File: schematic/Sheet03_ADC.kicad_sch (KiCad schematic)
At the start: 5 parts

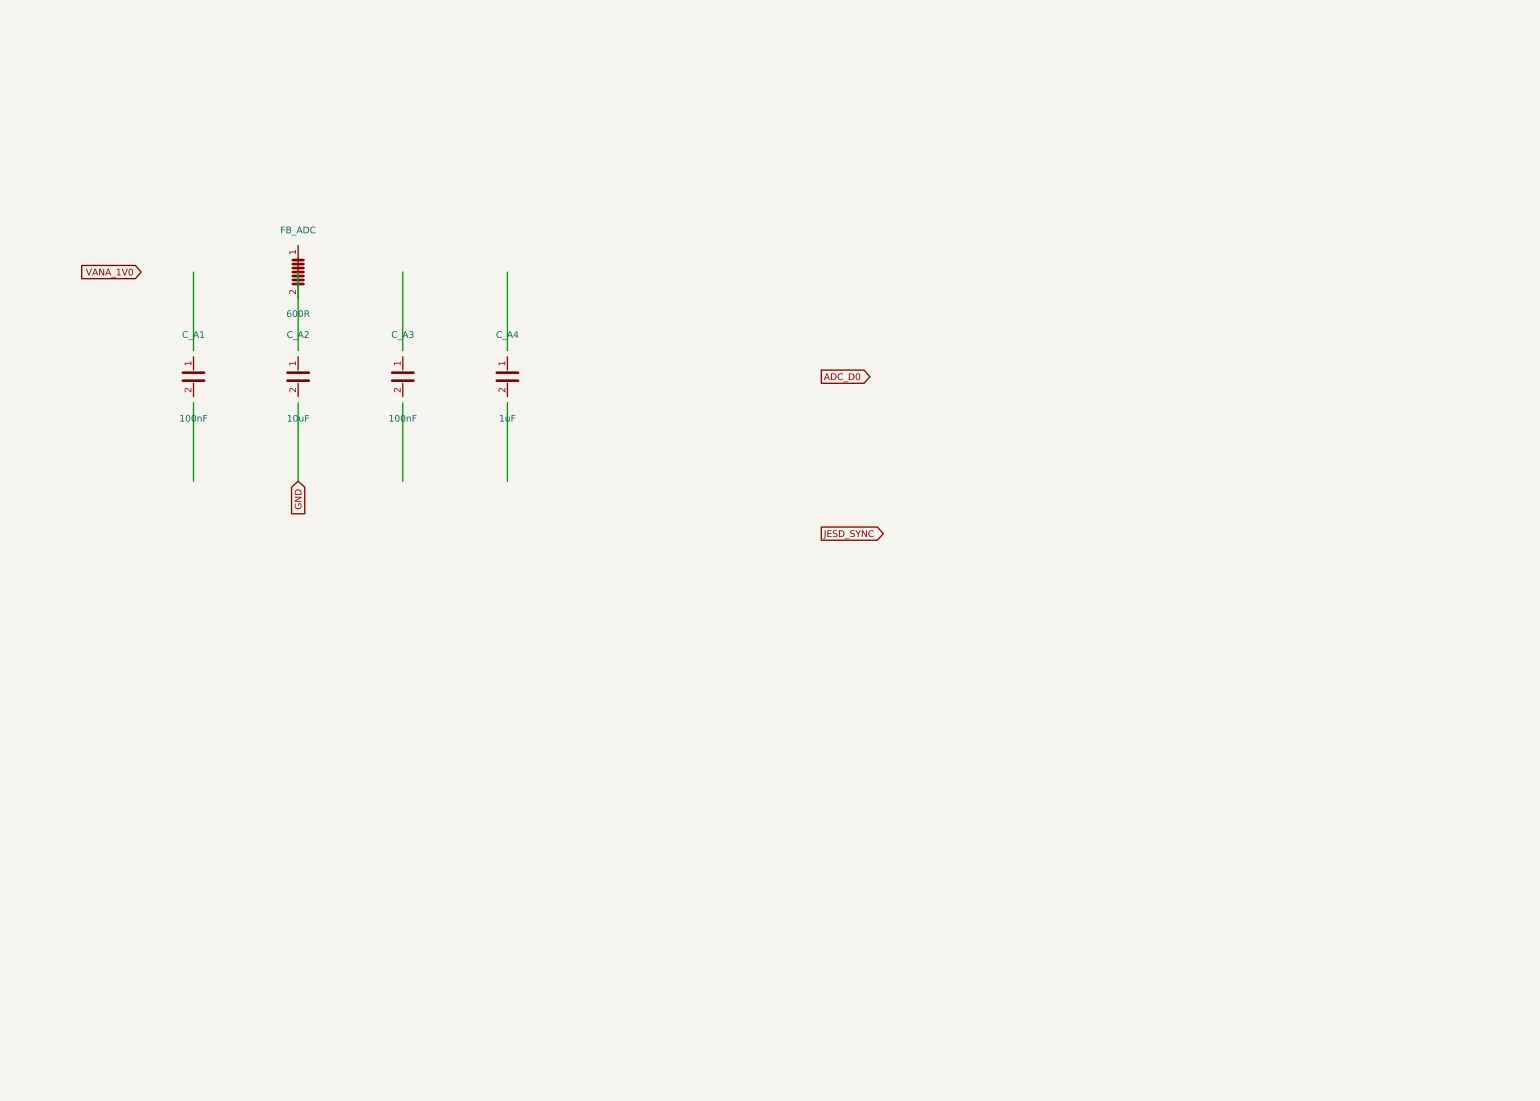
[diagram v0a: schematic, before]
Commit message: feat: real IC schematics with proper pin connections
- ADC12DJ5200-SP: 20 left pins (power, SPI, analog) + 21 right pins (JESD204C)
- XQRVC1902-SP: 19 left pins (power) + 30 right pins (JTAG, SPW, JESD, config)
- TPS7H5002-SP: 9 left + 7 right pins (buck converter 1.0V core)
- ISL70003ASEH: 7 left + 5 right (buck 1.8V/3.3V)
- LMX2615-SP: 8+8 pins (PLL synthesizer)
- LMK04832-SP: 12+12 pins (clock distributor)
- TPS7H1111-SP / TPS7H1121-SP: 3+3 pins (LDOs)
- TPS7H3014-SP: 4+4 pins (sequencer)
- INA214-SP: 3+2 pins (current sense)
- CVHD-950: 3+2 pins (VCXO)

Sheets:
- 02: SMA→50Ω match→anti-alias→ADC analog input
- 03: ADC decoupling, JESD outputs, SPI control
- 04: FPGA 14x decoupling caps, JTAG, SPW, JESD
- 05: Crystek→LMX2615→LMK04832→ADC+FPGA clock tree
- 06-09: Power input, TPS7H5002 buck 1.0V, ISL70003A buck 1.8V/3.3V
- 10-12: LDO 1.0V analog, 1.8V digital, 2.5V clock
- 13: 2x TPS7H3014 power sequencer
- 14: JTAG/SPW/UART connectors
- 15-17: Test points, decoupling, power tree diagram

All 17 sheets export via kicad-cli, merged PDF: 1.1MB
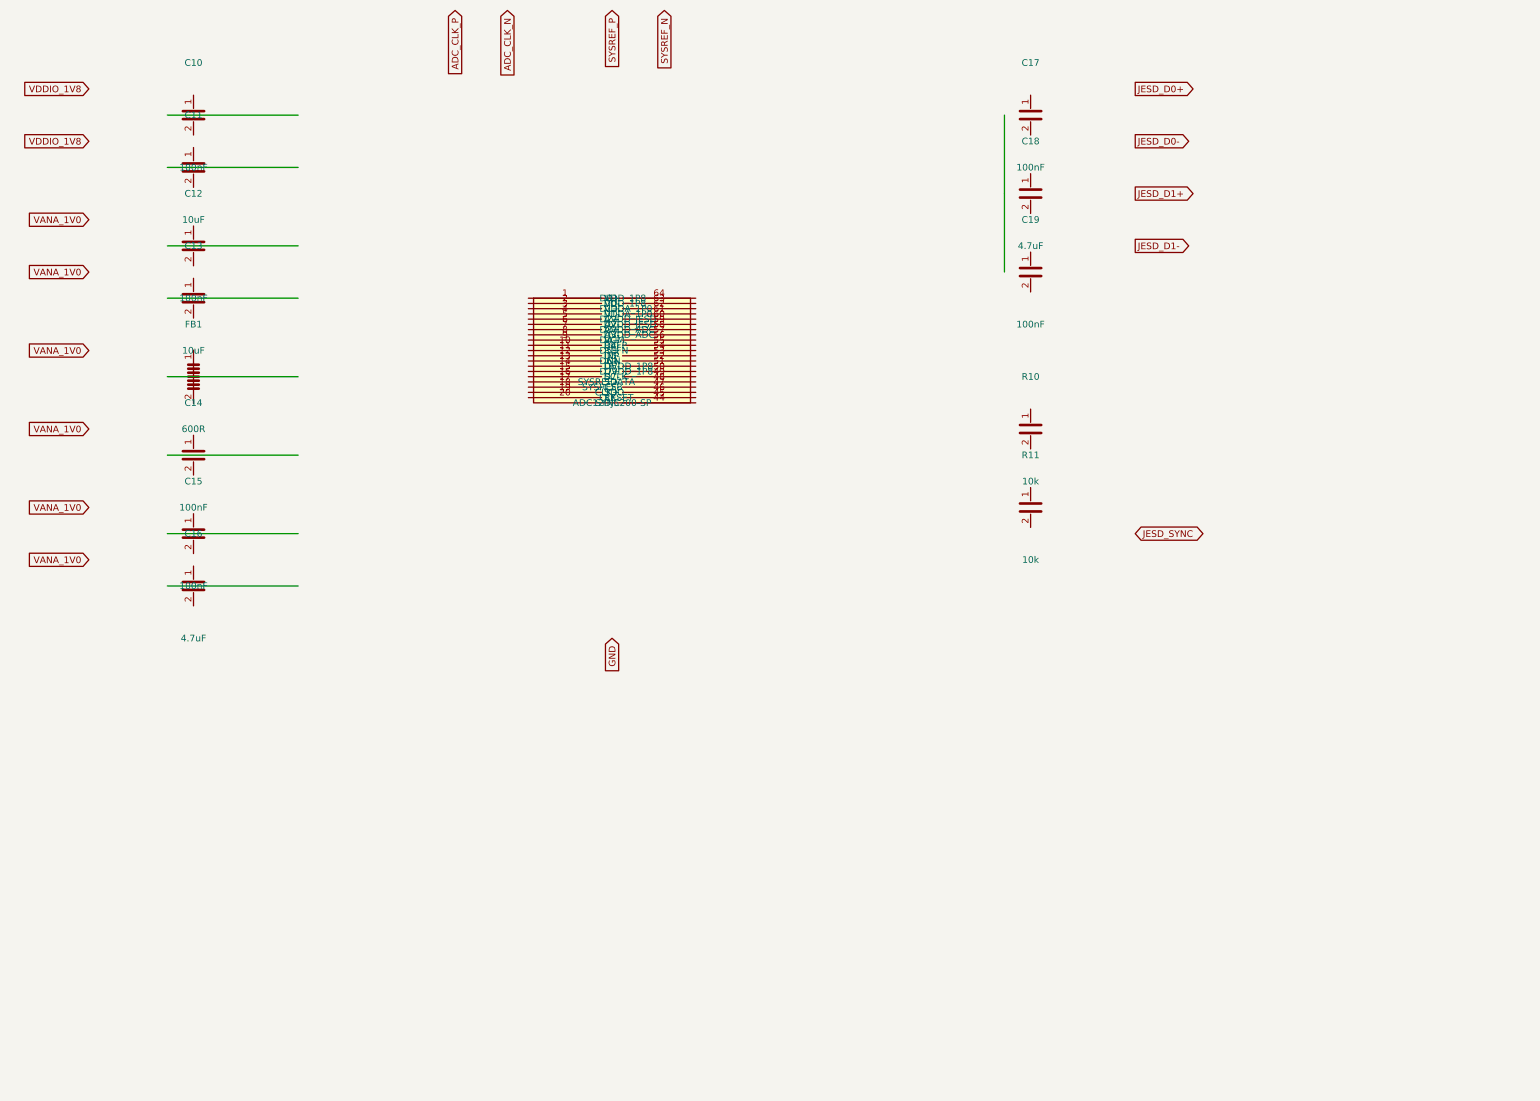
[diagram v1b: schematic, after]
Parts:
- removed C_A1, C_A3: 100nF, Capacitor_SMD:C_0402_1005Metric, symbol Device:C
- removed C_A2: 10uF, Capacitor_SMD:C_0603_1608Metric, symbol Device:C
- removed C_A4: 1uF, Capacitor_SMD:C_0402_1005Metric, symbol Device:C
- removed FB_ADC: 600R, Inductor_SMD:L_0402_1005Metric, symbol Device:FerriteBead
- added C10, C12, C14, C15, C17, C19: 100nF, C_0402, symbol Device:C
- added C11, C13: 10uF, C_0603, symbol Device:C
- added C16, C18: 4.7uF, C_0402, symbol Device:C
- added FB1: 600R, L_0402, symbol Device:FerriteBead
- added R10, R11: 10k, C_0402, symbol Device:C
- added U1: ADC12DJ5200-SP, QFN-64, symbol Custom:ADC12DJ5200-SP
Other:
- title: X-Band Digital Module 20x20cm -> X-Band ADC12DJ5200-SP

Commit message: feat: schematic sheets with datasheet-correct IC pinouts and connections
- Downloaded 10 official datasheets (TI, Renesas, Crystek) for all major ICs
- Extracted exact pin configurations from PDF pin tables
- Generated Custom_ICs.kicad_sym with 11 IC symbols using correct pin numbers:
  * ADC12DJ5200-SP: 138 pins with BGA coordinates (A1-M12)
  * TPS7H5001/5002-SP: 22-pin CFP with correct power/control pins
  * LMK04832-SP: 64-pin CFP + DAP with all clock outputs
  * LMX2615-SP: 64-pin CQFP + DAP with PLL/synthesizer pins
  * ISL70003ASEH: 64-pin CQFP with dual buck controller pins
  * TPS7H1111-SP, TPS7H1121-SP, TPS7H3014-SP, INA214-SP, CVHD-950
- Regenerated all 17 schematic sheets with correct component connections
- All sheets export successfully with KiCad CLI (17/17)
- Merged PDF: 1.3MB, 17 pages
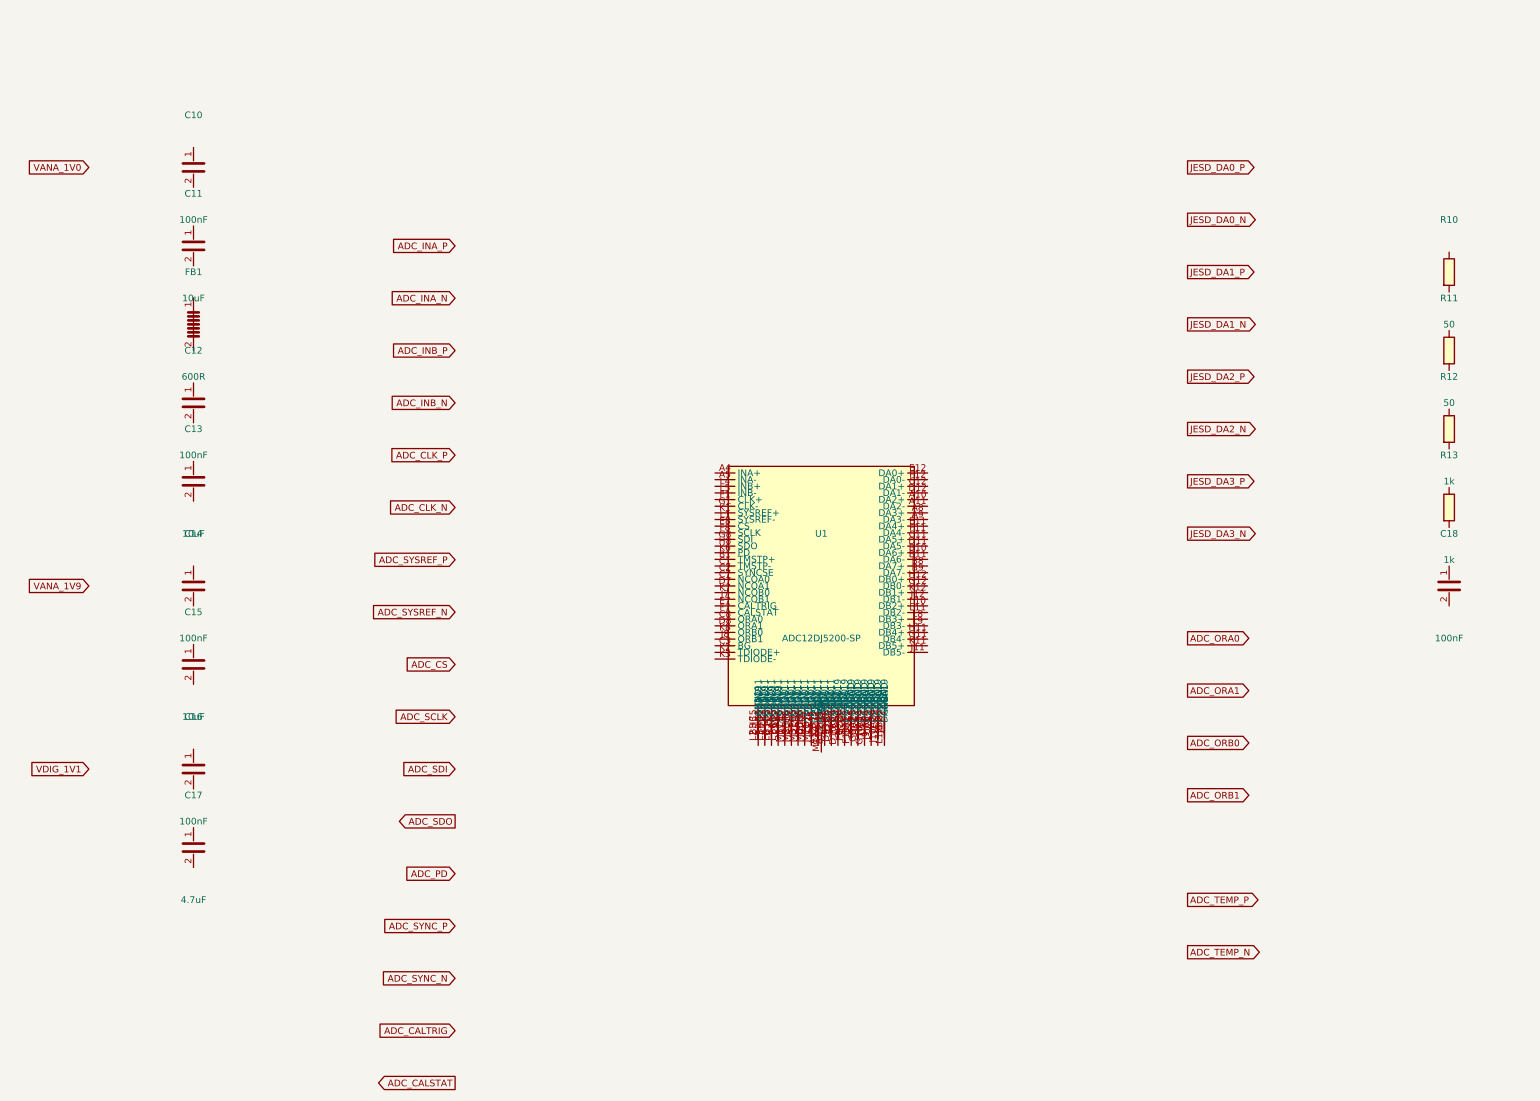
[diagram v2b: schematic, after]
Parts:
- removed C19: 100nF, C_0402, symbol Device:C
- removed R10, R11: 10k, C_0402, symbol Device:C
- added R10, R11: 50, R_0402, symbol Device:R
- added R12, R13: 1k, R_0402, symbol Device:R
- C15: value 100nF -> 10uF; footprint C_0402 -> C_0603
- C16, C18: value 4.7uF -> 100nF
- C17: value 100nF -> 4.7uF
- U1: footprint QFN-64 -> Package_BGA:BGA-144_12x12_8.0x8.0mm_P0.65mm

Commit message: feat: add 745 wire connections linking all IC pins to labels and power symbols
- Added stub wires from every component pin to net labels/global_labels
- Power pins connected to correct power symbols (GND, +1V0, +1V8, +3V3, etc.)
- Signal pins connected to labeled nets matching design spec
- Global labels for cross-sheet signals (JESD, SPI, clock, SpaceWire)
- Fixed missing +3V3 power symbol definitions in 5 sheets
- All 17 sheets export successfully with KiCad CLI (17/17 OK)
- Merged PDF: 3.1MB, 17 pages with visible wire connections
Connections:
- net ADC_PD: now also U1.C8 (ORA0)
- net ADC_SYNC_N: now also U1.E7 (CALTRIG)
- net ADC_SYNC_P: now also U1.F7 (CALSTAT)
- net ADC_SYSREF_N: now also U1.K2 (TDIODE+)
- net ADC_SYSREF_P: now also U1.K3 (TDIODE-)
- net ~: now reaches C11.1
- net ~: now also C10.1, C10.2, C11.2, C12.1, C12.2, C13.1, C13.2, C14.1, C14.2, C15.1, C15.2, C16.1, C16.2, C17.1, C17.2, C18.1, C18.2, FB1.1, FB1.2, R10.1, R10.2, R11.1, R11.2, R12.1, R12.2, R13.1, R13.2
- net FPGA_CAL_STAT: now reaches U1.B1 (TMSTP+)
- net FPGA_CAL_TRIG: now reaches U1.C1 (TMSTP-)
- net GND: now reaches U1.C2 (SYNCSE)
- net GND: now also U1.C7 (NCOA0), U1.D7 (NCOA1), U1.J7 (NCOB1), U1.K7 (NCOB0)
- net CS: now reaches U1.C3 (BG)
- net SPI_MISO: now reaches U1.D8 (ORA1)
- net ADC_VBG: now reaches U1.E8 (CS)
- net FPGA_ORB1: now reaches U1.F8 (SCLK)
- net FPGA_ORB0: now reaches U1.G8 (SDI)
- net FPGA_ORA1: now reaches U1.H8 (SDO)
- net SPI_SCK: now reaches U1.J8 (ORB1)
- net TEMP_DIODE_N: now reaches U1.K1 (SYSREF+)
- net FPGA_ORA0: now reaches U1.K6 (PD)
- net SPI_MOSI: now reaches U1.K8 (ORB0)
- net TEMP_DIODE_P: now reaches U1.L1 (SYSREF-)
